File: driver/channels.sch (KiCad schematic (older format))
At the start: 4 parts, among them J201 A_1_32, J202 K_1_32, J203 A_33_64, J204 K_33_64

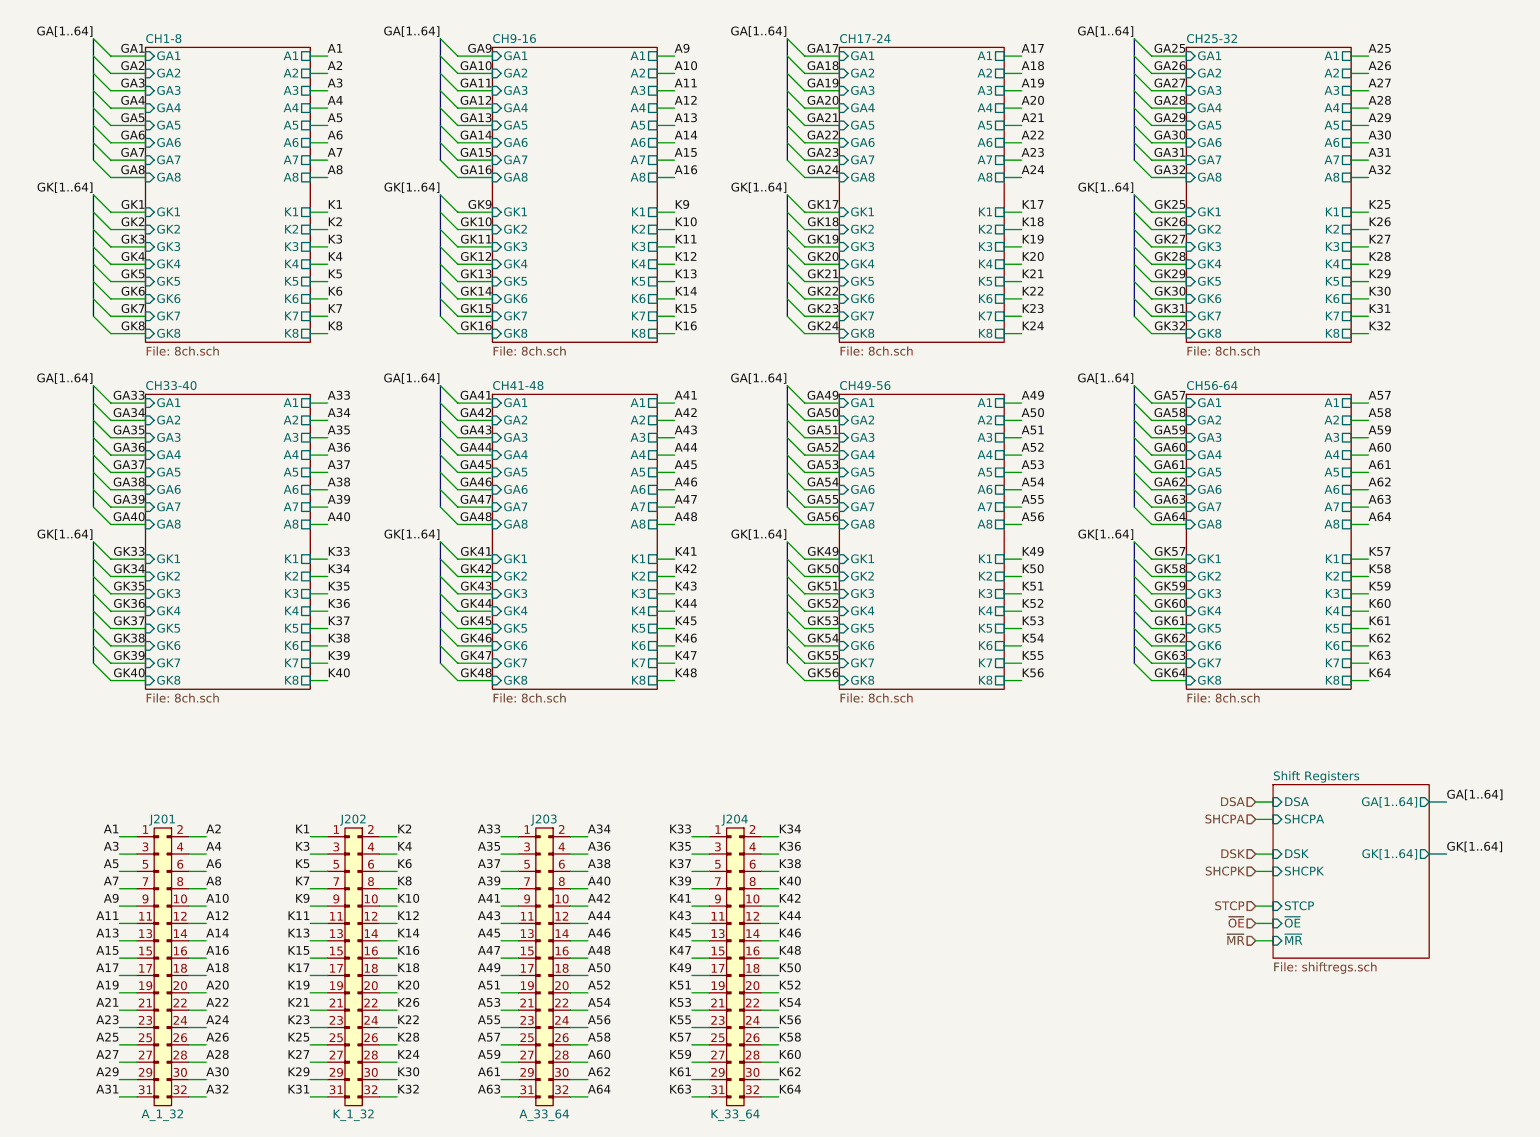
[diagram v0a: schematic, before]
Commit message: Finish sch, start PCB
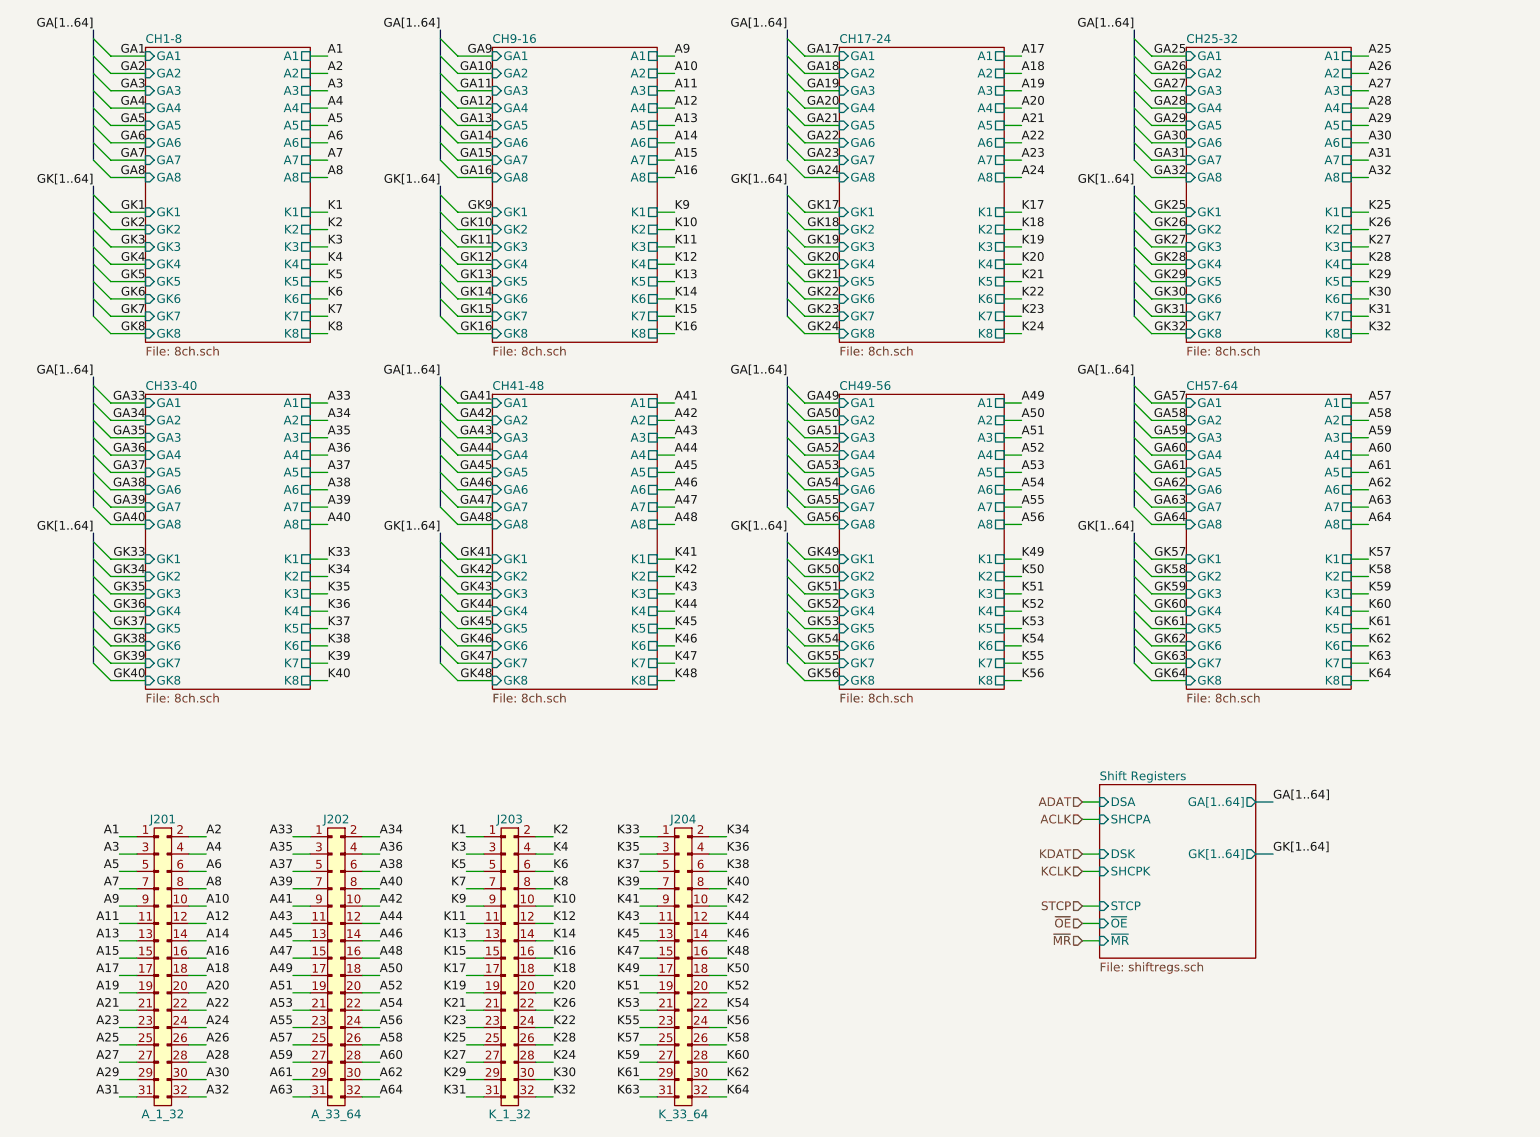
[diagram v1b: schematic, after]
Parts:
- J201, J204: footprint (none) -> agg:DIL-254P-32; Farnell (none) -> 2856270; MPN (none) -> IPL1-116-01-L-D-RA-K
- J202: renamed from J203; footprint (none) -> agg:DIL-254P-32; Farnell (none) -> 2856270; MPN (none) -> IPL1-116-01-L-D-RA-K
- J203: renamed from J202; footprint (none) -> agg:DIL-254P-32; Farnell (none) -> 2856270; MPN (none) -> IPL1-116-01-L-D-RA-K
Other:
- moved on the sheet: J202, J203, J204

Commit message: WIP PCB
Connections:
- net K1: now also J203.31; no longer J203.1
- net K10: now also J203.24; no longer J203.10
- net K11: now also J203.21; no longer J203.11
- net K12: now also J203.22; no longer J203.12
- net K13: now also J203.19; no longer J203.13
- net K14: now also J203.20; no longer J203.14
- net K15: now also J203.17; no longer J203.15
- net K16: now also J203.18; no longer J203.16
- net K17: now also J203.15; no longer J203.17
- net K18: now also J203.16; no longer J203.18
- net K19: now also J203.13; no longer J203.19
- net K2: now also J203.32; no longer J203.2
- net K20: now also J203.14; no longer J203.20
- net K21: now also J203.11; no longer J203.21
- net K22: now also J203.10; no longer J203.24
- net K23: now also J203.9; no longer J203.23
- net K24: now also J203.6; no longer J203.28
- net K25: now also J203.7; no longer J203.25
- net K26: now also J203.12; no longer J203.22
- net K27: now also J203.5; no longer J203.27
- net K28: now also J203.8; no longer J203.26
- net K29: now also J203.3; no longer J203.29
- net K3: now also J203.29; no longer J203.3
- net K30: now also J203.4; no longer J203.30
- net K31: now also J203.1; no longer J203.31
- net K32: now also J203.2; no longer J203.32
- net K33: now also J204.31; no longer J204.1
- net K34: now also J204.32; no longer J204.2
- net K35: now also J204.29; no longer J204.3
- net K36: now also J204.30; no longer J204.4
- net K37: now also J204.27; no longer J204.5
- net K38: now also J204.28; no longer J204.6
- net K39: now also J204.25; no longer J204.7
- net K4: now also J203.30; no longer J203.4
- net K40: now also J204.26; no longer J204.8
- net K41: now also J204.23; no longer J204.9
- net K42: now also J204.24; no longer J204.10
- net K43: now also J204.21; no longer J204.11
- net K44: now also J204.22; no longer J204.12
- net K45: now also J204.19; no longer J204.13
- net K46: now also J204.20; no longer J204.14
- net K47: now also J204.17; no longer J204.15
- net K48: now also J204.18; no longer J204.16
- net K49: now also J204.15; no longer J204.17
- net K5: now also J203.27; no longer J203.5
- net K50: now also J204.16; no longer J204.18
- net K51: now also J204.13; no longer J204.19
- net K52: now also J204.14; no longer J204.20
- net K53: now also J204.11; no longer J204.21
- net K54: now also J204.12; no longer J204.22
- net K55: now also J204.9; no longer J204.23
- net K56: now also J204.10; no longer J204.24
- net K57: now also J204.7; no longer J204.25
- net K58: now also J204.8; no longer J204.26
- net K59: now also J204.5; no longer J204.27
- net K6: now also J203.28; no longer J203.6
- net K60: now also J204.6; no longer J204.28
- net K61: now also J204.3; no longer J204.29
- net K62: now also J204.4; no longer J204.30
- net K63: now also J204.1; no longer J204.31
- net K64: now also J204.2; no longer J204.32
- net K7: now also J203.25; no longer J203.7
- net K8: now also J203.26; no longer J203.8
- net K9: now also J203.23; no longer J203.9
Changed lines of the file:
@@
 F 1 "A_1_32" H 2100 3850 50  0000 C CNN
 F 2 "agg:DIL-254P-32" H 2150 5450 50  0001 C CNN
-F 3 "" H 2150 5450 50  0001 C CNN
+F 3 "http://suddendocs.samtec.com/catalog_english/ipl1.pdf" H 2150 5450 50  0001 C CNN
 F 4 "IPL1-116-01-L-D-RA-K" H 2150 5450 50  0001 C CNN "MPN"
 F 5 "2856270" H 2150 5450 50  0001 C CNN "Farnell"
@@
 F 1 "A_33_64" H 3100 3850 50  0000 C CNN
 F 2 "agg:DIL-254P-32" H 3150 5450 50  0001 C CNN
-F 3 "" H 3150 5450 50  0001 C CNN
+F 3 "http://suddendocs.samtec.com/catalog_english/ipl1.pdf" H 3150 5450 50  0001 C CNN
 F 4 "IPL1-116-01-L-D-RA-K" H 3150 5450 50  0001 C CNN "MPN"
 F 5 "2856270" H 3150 5450 50  0001 C CNN "Farnell"
@@
 L agg-kicad:CONN_02x16 J?
 U 1 1 637212A4
-P 5150 5450
+P 5150 6950
 AR Path="/637212A4" Ref="J?"  Part="1"
 AR Path="/636F06DD/637212A4" Ref="J204"  Part="1"
-F 0 "J204" H 5100 5550 50  0000 C CNN
-F 1 "K_33_64" H 5100 3850 50  0000 C CNN
-F 2 "agg:DIL-254P-32" H 5150 5450 50  0001 C CNN
-F 3 "" H 5150 5450 50  0001 C CNN
-F 4 "IPL1-116-01-L-D-RA-K" H 5150 5450 50  0001 C CNN "MPN"
-F 5 "2856270" H 5150 5450 50  0001 C CNN "Farnell"
-	1    5150 5450
-	1    0    0    -1
+F 0 "J204" H 5100 7050 50  0000 C CNN
+F 1 "K_33_64" H 5100 5350 50  0000 C CNN
+F 2 "agg:DIL-254P-32" H 5150 6950 50  0001 C CNN
+F 3 "http://suddendocs.samtec.com/catalog_english/ipl1.pdf" H 5150 6950 50  0001 C CNN
+F 4 "IPL1-116-01-L-D-RA-K" H 5150 6950 50  0001 C CNN "MPN"
+F 5 "2856270" H 5150 6950 50  0001 C CNN "Farnell"
+	1    5150 6950
+	1    0    0    1
 $EndComp
 $Sheet
@@
 L agg-kicad:CONN_02x16 J?
 U 1 1 637218E9
-P 4150 5450
+P 4150 6950
 AR Path="/637218E9" Ref="J?"  Part="1"
 AR Path="/636F06DD/637218E9" Ref="J203"  Part="1"
-F 0 "J203" H 4100 5550 50  0000 C CNN
-F 1 "K_1_32" H 4100 3850 50  0000 C CNN
-F 2 "agg:DIL-254P-32" H 4150 5450 50  0001 C CNN
-F 3 "" H 4150 5450 50  0001 C CNN
-F 4 "IPL1-116-01-L-D-RA-K" H 4150 5450 50  0001 C CNN "MPN"
-F 5 "2856270" H 4150 5450 50  0001 C CNN "Farnell"
-	1    4150 5450
-	1    0    0    -1
+F 0 "J203" H 4100 7050 50  0000 C CNN
+F 1 "K_1_32" H 4100 5350 50  0000 C CNN
+F 2 "agg:DIL-254P-32" H 4150 6950 50  0001 C CNN
+F 3 "http://suddendocs.samtec.com/catalog_english/ipl1.pdf" H 4150 6950 50  0001 C CNN
+F 4 "IPL1-116-01-L-D-RA-K" H 4150 6950 50  0001 C CNN "MPN"
+F 5 "2856270" H 4150 6950 50  0001 C CNN "Farnell"
+	1    4150 6950
+	1    0    0    1
 $EndComp
 Entry Wire Line
@@
 Wire Wire Line
 	3800 3850 4000 3850
-Wire Wire Line
-	3800 3950 4000 3950
-Wire Wire Line
-	3800 4050 4000 4050
-Wire Wire Line
-	3800 4150 4000 4150
-Wire Wire Line
-	3800 4250 4000 4250
-Wire Wire Line
-	3800 4350 4000 4350
-Wire Wire Line
-	3800 4450 4000 4450
-Wire Wire Line
-	3800 4550 4000 4550
 Wire Wire Line
 	7800 950  8000 950
@@
 Text Label 7700 3700 2    50   ~ 0
 GK[1..64]
+Wire Wire Line
+	3800 3950 4000 3950
+Wire Wire Line
+	3800 4050 4000 4050
+Wire Wire Line
+	3800 4150 4000 4150
+Wire Wire Line
+	3800 4250 4000 4250
+Wire Wire Line
+	3800 4350 4000 4350
+Wire Wire Line
+	3800 4450 4000 4450
+Wire Wire Line
+	3800 4550 4000 4550
 Wire Bus Line
 	1700 3700 1700 4450

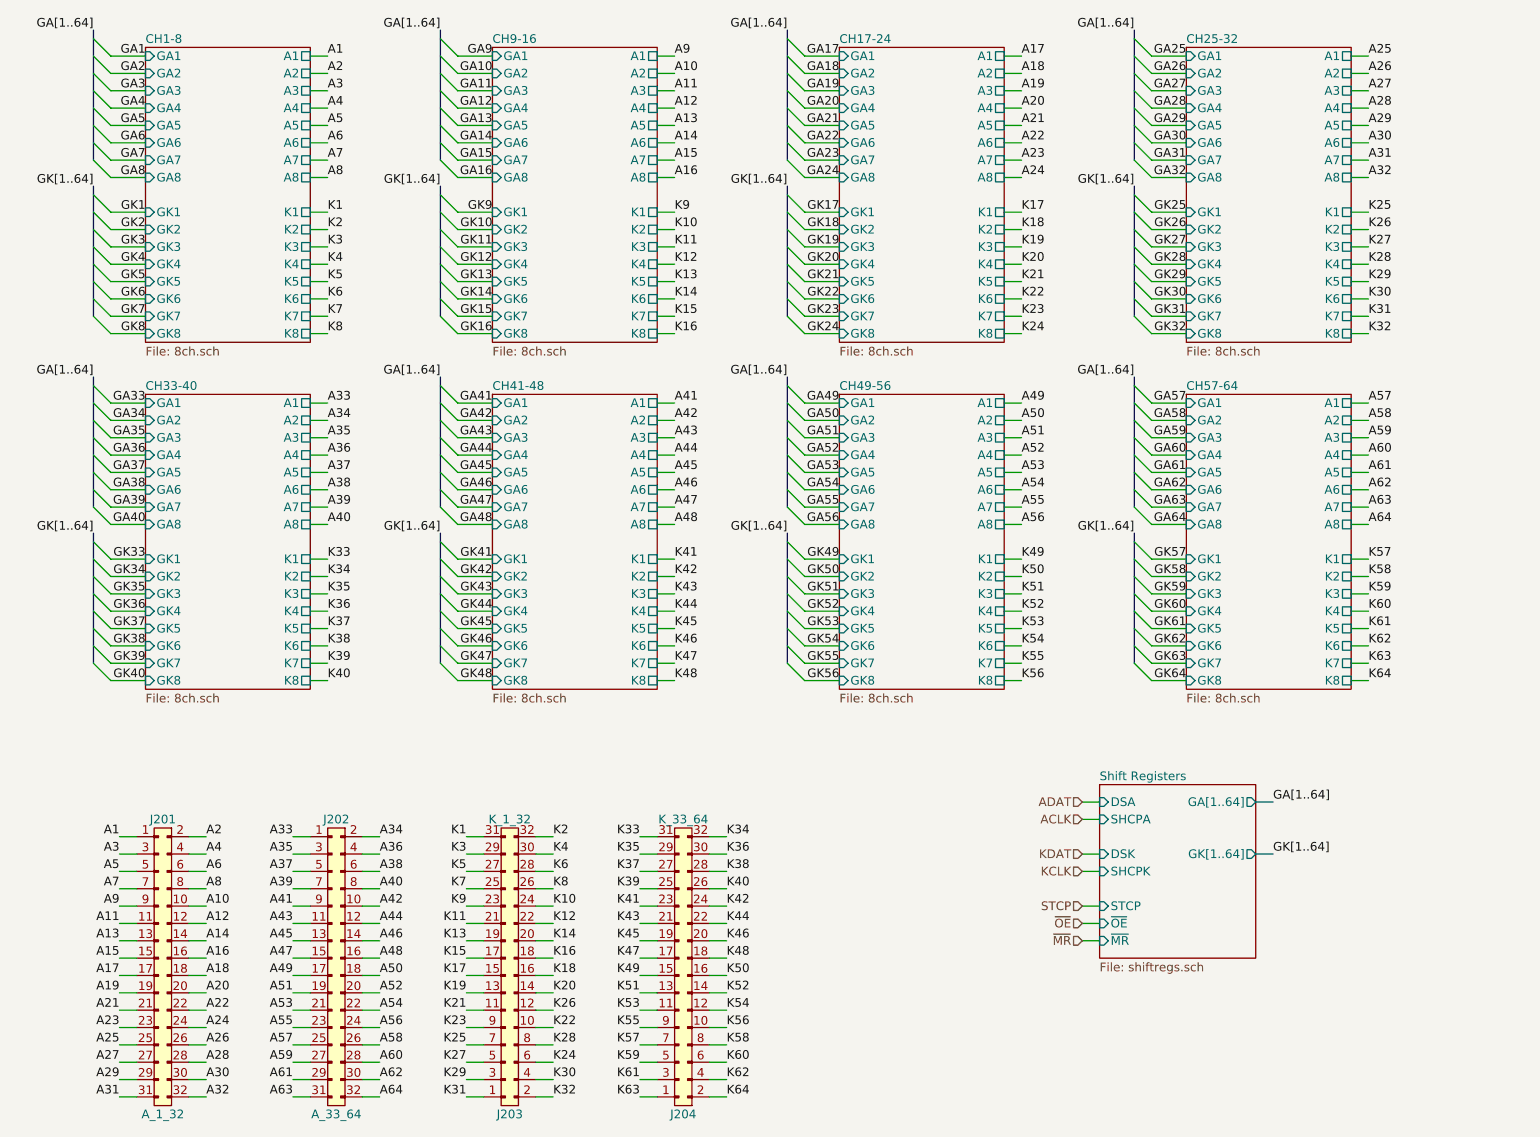
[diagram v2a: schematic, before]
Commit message: Start work on 32ch board
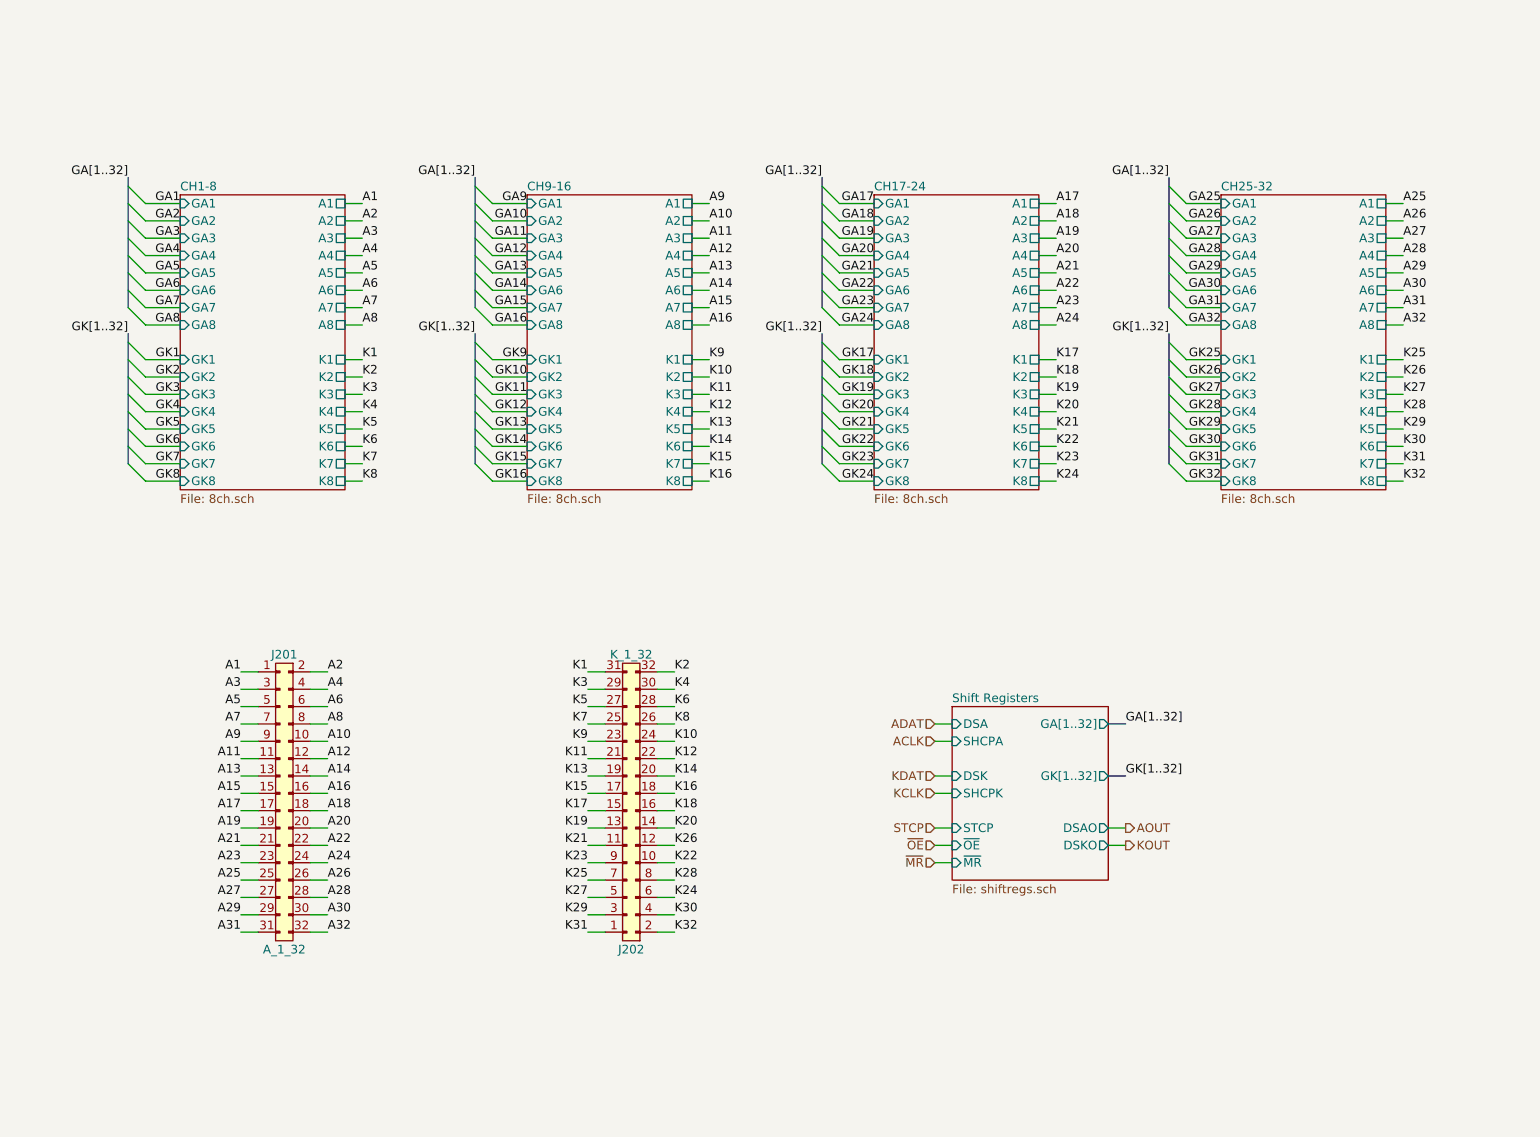
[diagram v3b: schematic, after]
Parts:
- removed J202: A_33_64, agg:DIL-254P-32, symbol agg-kicad:CONN_02x16
- removed J204: K_33_64, agg:DIL-254P-32, symbol agg-kicad:CONN_02x16
- renumbered J203 to J202
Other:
- moved on the sheet: J201, J202

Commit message: more layout work
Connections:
- net K22: now also J202.12; no longer J202.10
- net K24: now also J202.10; no longer J202.6
- net K26: now also J202.8; no longer J202.12
- net K28: now also J202.6; no longer J202.8
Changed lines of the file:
@@
 Text Label 5050 5400 0    50   ~ 0
 K20
+Text Label 5050 5500 0    50   ~ 0
+K22
 Text Label 5050 5600 0    50   ~ 0
-K22
-Text Label 5050 5800 0    50   ~ 0
 K24
 Text Label 4550 5300 2    50   ~ 0
@@
 Text Label 4550 5600 2    50   ~ 0
 K23
-Text Label 5050 5500 0    50   ~ 0
+Text Label 5050 5700 0    50   ~ 0
 K26
-Text Label 5050 5700 0    50   ~ 0
+Text Label 5050 5800 0    50   ~ 0
 K28
 Text Label 5050 5900 0    50   ~ 0
